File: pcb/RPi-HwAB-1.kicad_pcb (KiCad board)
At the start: 8 copper layers, 65 x 56 mm, 135 parts, among them J1 TC2030, J2 GPIO, J3 Hirose_FH12-16S, U1 CAT24C256, U10 INA230AIRGTR, U2 TPSM82903, U3 MAX20029, U4 XC7A100T-FGG484, U6 MT41K256M16TW-107:P TR, U7 MX25L12835F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

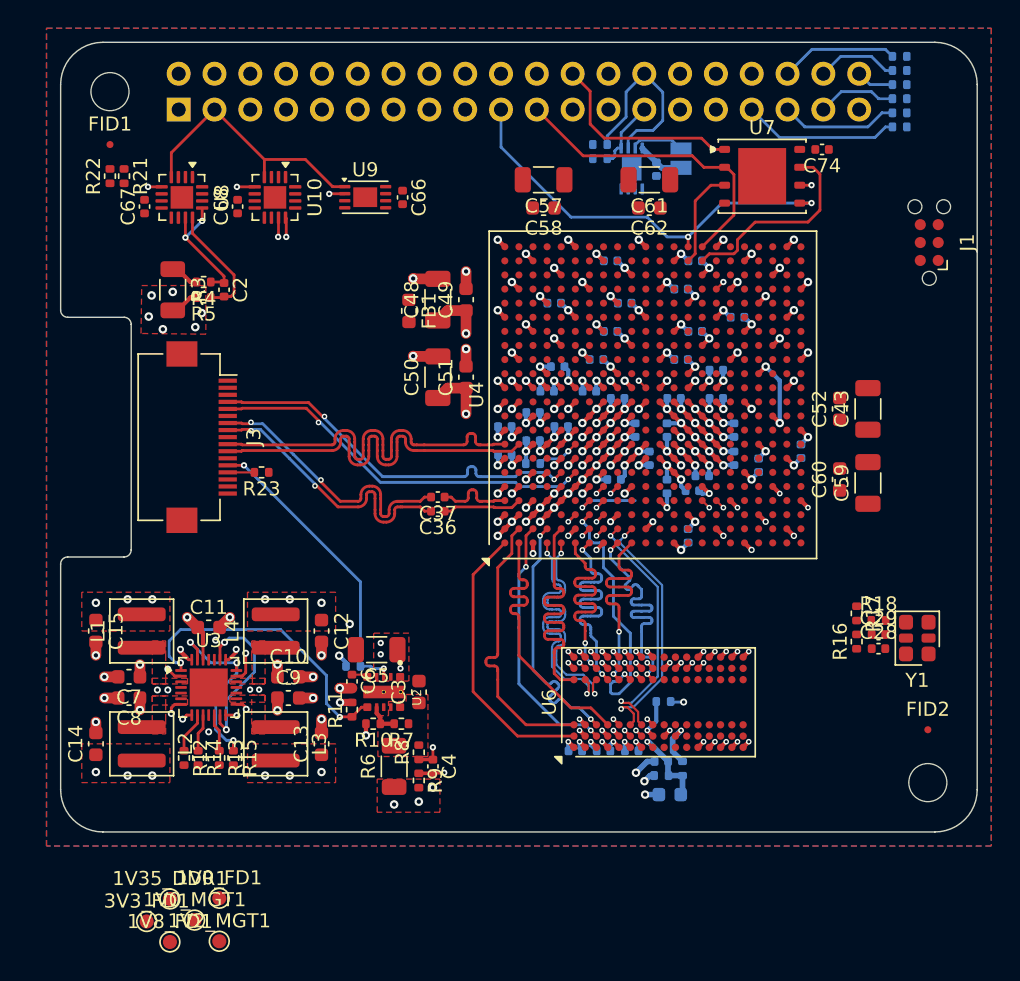
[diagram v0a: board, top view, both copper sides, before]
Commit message: power plane apportionment redid power planes, clearance to 0.2mm, most on l5, some on l6
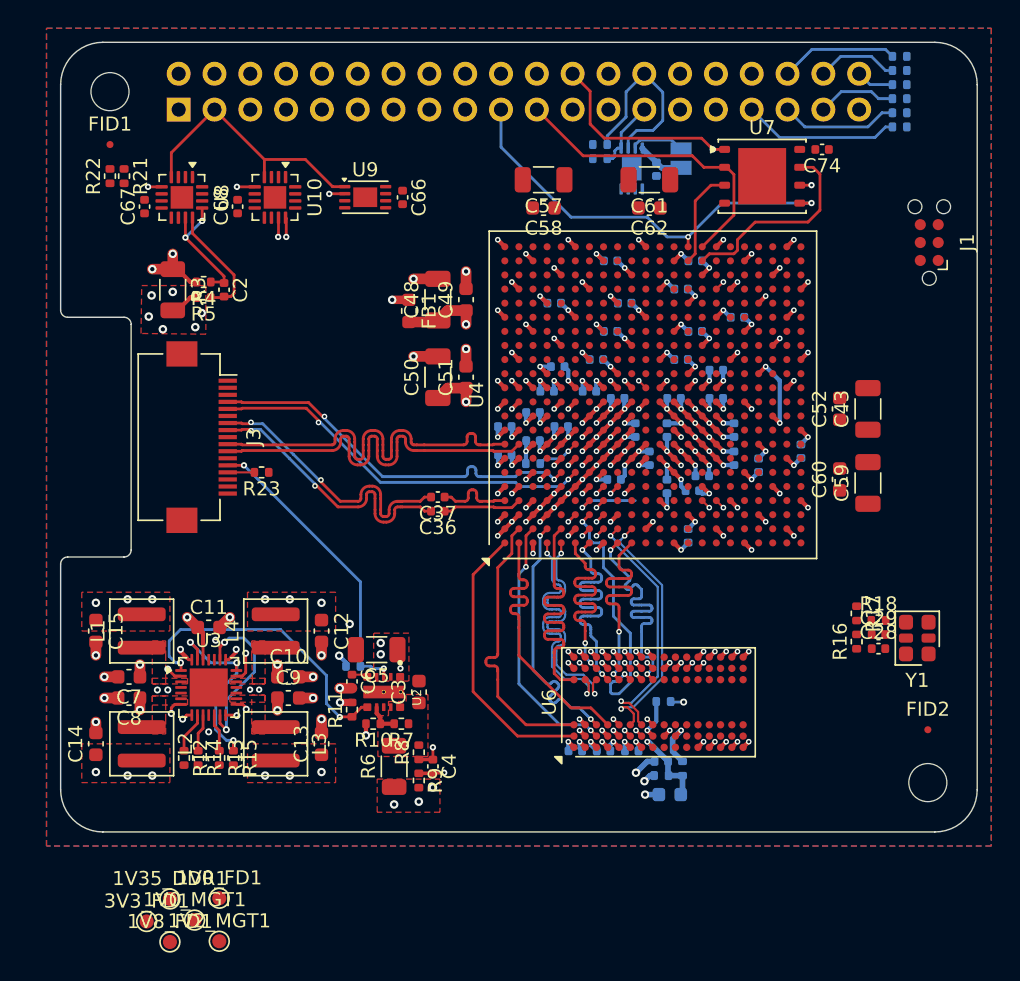
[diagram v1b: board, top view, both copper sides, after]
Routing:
- net /Connectors/5V0: track 2.06 -> 4.60 mm, vias 0 -> 2
- net /Main Power/1V0_MGT: track 9.67 -> 11.1 mm
- net /Main Power/1V0_FD: track 24.7 -> 25.9 mm, vias 21 -> 22
- net /Main Power/1V2_MGT: track 12.7 -> 11.8 mm
- net Net-(U6-V_{REFCA}): track 14.7 -> 14.1 mm
- added copper zone on In4.Cu, net /Connectors/5V0
- added copper zone on In5.Cu, net /Main Power/1V8_FD
- removed copper zone on In4.Cu, net /Main Power/1V8_FD

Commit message: ok
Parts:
- added FID3: Fiducial, Fiducial:Fiducial_1mm_Mask3mm, F.Cu at (103.0, 60.0)
- FID1, FID2: footprint Fiducial:Fiducial_0.5mm_Mask1mm -> Fiducial:Fiducial_1mm_Mask3mm
- moved FID1 69.6 mm to (156.0, 97.0)
- moved FID2 45.8 mm to (162.0, 47.0)
- moved 1V0_MGT1 44.4 mm to (122.7, 63.9)
- moved 1V2_MGT1 26.3 mm to (118.5, 82.5)
- moved 1V8_FD1 25.8 mm to (102.5, 82.5)
- moved 1V0_FD1 18.2 mm to (128.0, 97.5)
- moved 3V3_FD1 15.5 mm to (118.5, 97.0)
- moved 1V35_DDR1 9.36 mm to (102.5, 97.0)
- moved C43 2.28 mm to (157.2, 67.7)
- moved C52 2.28 mm to (155.2, 67.7)
- moved C59 2.28 mm to (157.2, 73.0)
- moved C60 2.28 mm to (155.2, 72.7)
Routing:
- net /Main Power/3V3_PG: track 2.67 -> 64.0 mm, vias 0 -> 1
- net /Connectors/PCIE.RST_B: track 0.00 -> 50.6 mm, vias 0 -> 2
- net /FPGA/FPGA 34, 35/A1: track 0.00 -> 18.2 mm
- net /FPGA/FPGA 34, 35/DDR_CK_P: track 0.00 -> 13.2 mm, vias 0 -> 2
- net /FPGA/FPGA 34, 35/DDR_CK_N: track 0.00 -> 12.1 mm, vias 0 -> 2
- net /FPGA/FPGA 34, 35/DDR_CKE: track 0.00 -> 10.7 mm
- net /FPGA/FPGA 34, 35/A8: track 0.00 -> 9.71 mm
- net /FPGA/FPGA 34, 35/DDR_BA1: track 0.00 -> 7.54 mm, vias 0 -> 1
- net /Main Power/Quad Buck/1V2_PG: track 14.7 -> 21.9 mm, vias 2 -> 3
- net /FPGA/FPGA 34, 35/DDR_BA0: track 0.00 -> 6.62 mm
- net /FPGA/FPGA 34, 35/A14: track 0.00 -> 4.49 mm
- net /FPGA/FPGA 34, 35/DDR_BA2: track 0.00 -> 4.27 mm
- net /FPGA/FPGA 34, 35/A2: track 0.00 -> 3.91 mm
- net /Main Power/5V0_N: track 15.2 -> 18.2 mm, vias 19 -> 23
- net /FPGA/FPGA 34, 35/A12: track 0.00 -> 2.77 mm, vias 0 -> 1
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- added copper zone on F.Cu, net /Connectors/5V0
- added copper zone on In5.Cu, net /Connectors/5V0
- added copper zone on In5.Cu, net 3V3_RPi
